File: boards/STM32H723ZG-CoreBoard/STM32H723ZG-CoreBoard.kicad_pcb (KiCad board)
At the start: 4 copper layers, 84 x 84 mm, 48 parts, among them J1 USB-C, J2 PORT_L, J3 PORT_B, J4 PORT_R, J5 PORT_T, J6 SWD, SW1 RESET, SW2 BOOT0, U1 STM32H723ZGT6, U2 AP2112K-3.3, Y1 25MHz, Y2 32.768kHz

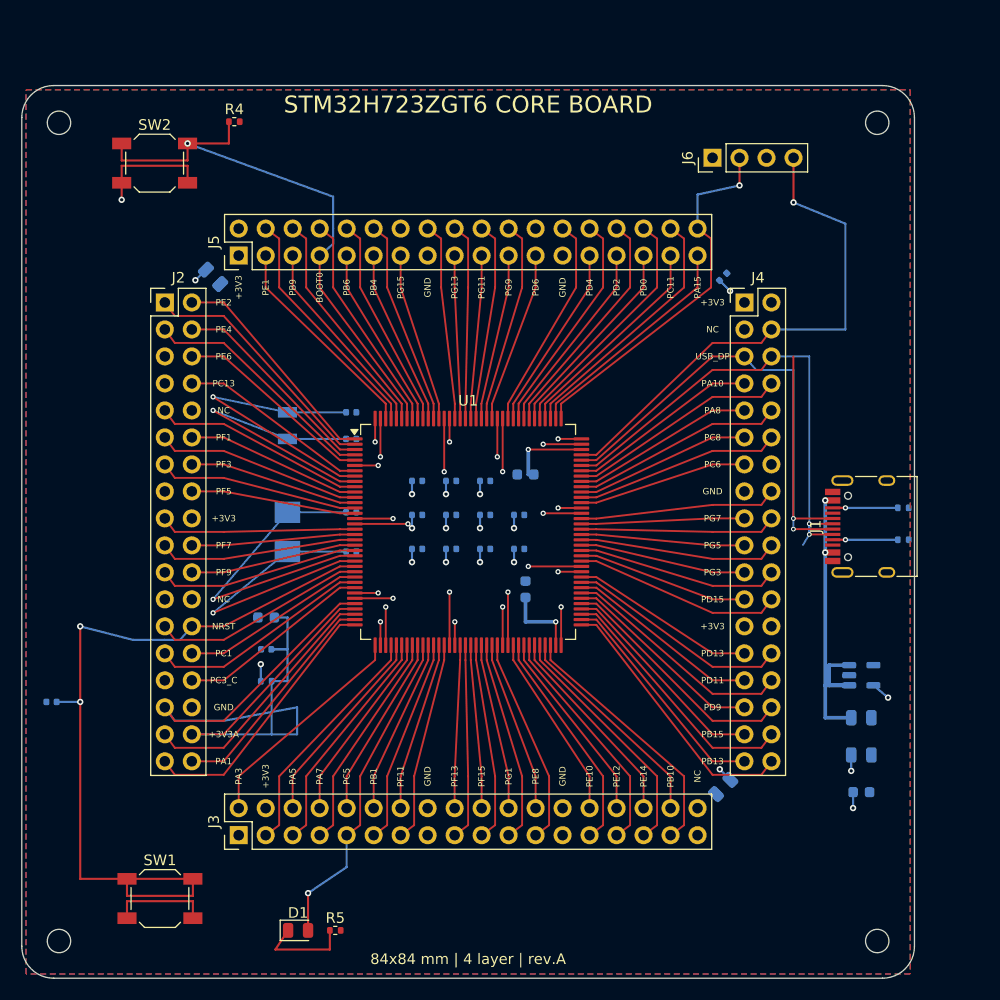
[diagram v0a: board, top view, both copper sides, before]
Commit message: Довести H723 до KiCad 10: разъём прошивки, STDC14, переразметка верхнего кольца
Плата H723 пересобрана в формате KiCad 10 и подтянута к раскладке G474.

Плата:
- разъём прошивки J6 - 1x10 с распиновкой WeAct, развёрнут 5V к востоку,
  SWO садится на PB3 прямой дорожкой;
- добавлен J7 - STDC14 (2x7, 1.27 мм), штатный разъём ST-LINK V3. Стоит
  вертикально сигнальным рядом к J6: строки веера идут по строкам падов и
  между собой не пересекаются, а расходятся по слоям;
- USB-C стоит на плате целиком, D+/D- заведены на PA11/PA12;
- кнопки RST и BOOT0 собраны в колонку у левого края, R4 - вплотную к SW2;
- светодиод и резистор развёрнуты под 45 градусов в углу между J2 и J3;
- подписаны все 144 контакта гребёнок и номиналы всех компонентов.

Генератор:
- gen/kicadenv.py - поиск библиотек KiCad на любой ОС и различия API 7/10;
- gen/export.py - гербера, сверловка, pos.csv, PDF и архив через kicad-cli;
- сборка платы больше не зависит от системных библиотек: футпринты уходят в
  auto_probe.pretty рядом с платой;
- kigen.py: разбор многострочной формы pin_names/pin_numbers KiCad 10 -
  из-за неё поверх номеров контактов печатались имена;
- crtyd.py считает пересечение реальных полигонов, а не описанных
  прямоугольников; drc.py не считает нарушением зазор ровно по правилу.

Проверки H723: DRC KiCad 0 нарушений, 0 несоединённых, 0 расхождений со
схемой; собственный контроль зазоров 0, courtyard 0, шелкография 0.
Файлы платы G474 не тронуты, правки в build_g474.py - только переносимость.

Co-Authored-By: Claude Opus 5 <noreply@anthropic.com>
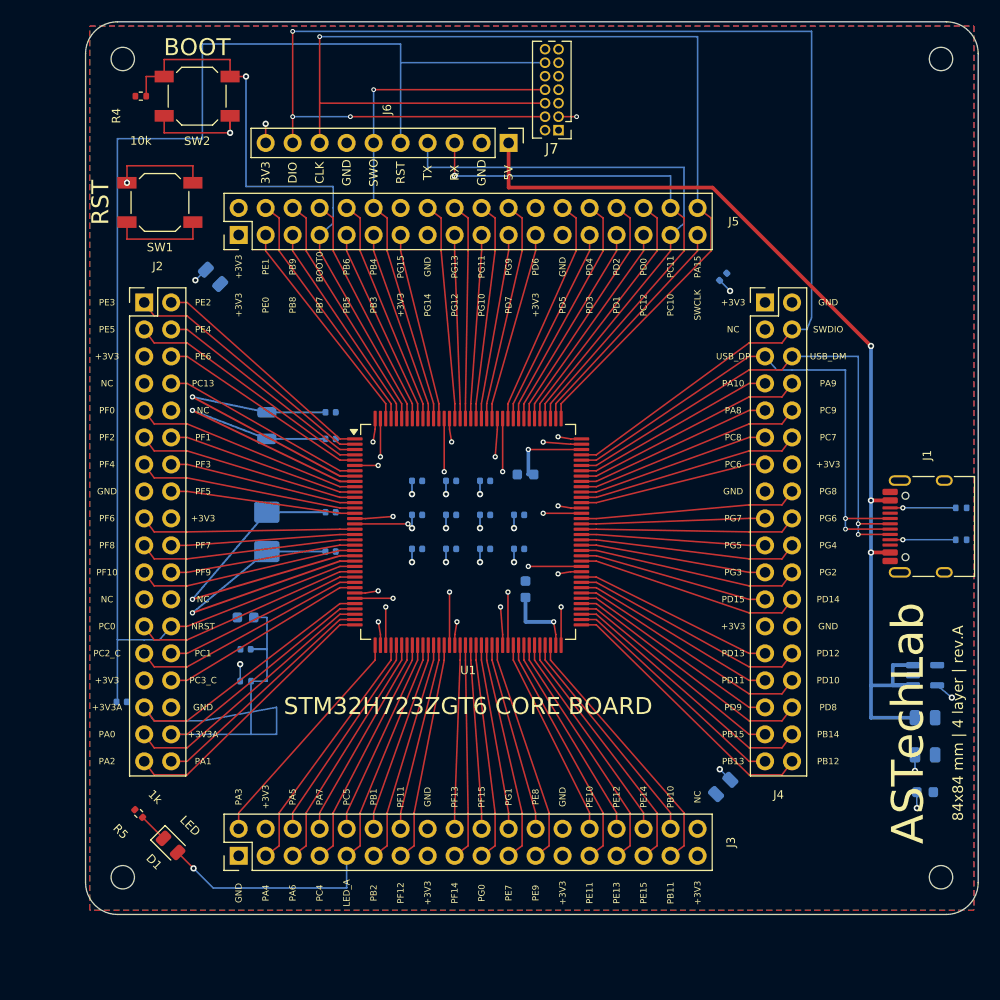
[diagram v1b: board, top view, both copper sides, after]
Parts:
- added J7: STDC14, auto_probe:PinHeader_2x07_P1.27mm_Vertical, F.Cu at (158.5, 62.2)
- C1, C10, C11, C2, C3, C4, C5, C6, C60, C61, C62, C63, C7, C70, C74, C77, C8, C9: footprint C_0402_1005Metric -> auto_probe:C_0402_1005Metric
- C50, C51, C75, C76: footprint C_0805_2012Metric -> auto_probe:C_0805_2012Metric
- C52, C71, C72, C73: footprint C_0603_1608Metric -> auto_probe:C_0603_1608Metric
- D1: value USER -> LED; footprint LED_0805_2012Metric -> auto_probe:LED_0805_2012Metric
- H1, H2, H3, H4: footprint MountingHole_2.2mm_M2 -> auto_probe:MountingHole_2.2mm_M2
- J1: footprint USB_C_Receptacle_HRO_TYPE-C-31-M-12 -> auto_probe:USB_C_Receptacle_HRO_TYPE-C-31-M-12
- J2, J3, J4, J5: footprint PinHeader_2x18_P2.54mm_Vertical -> auto_probe:PinHeader_2x18_P2.54mm_Vertical
- J6: value SWD -> DEBUG; footprint PinHeader_1x04_P2.54mm_Vertical -> auto_probe:PinHeader_1x10_P2.54mm_Vertical
- R1, R2, R3, R4, R5: footprint R_0402_1005Metric -> auto_probe:R_0402_1005Metric
- SW1, SW2: footprint SW_SPST_SKQG_WithoutStem -> auto_probe:SW_SPST_SKQG_WithoutStem
- U1: footprint LQFP-144_20x20mm_P0.5mm -> auto_probe:LQFP-144_20x20mm_P0.5mm
- U2: footprint SOT-23-5 -> auto_probe:SOT-23-5
- Y1: footprint Crystal_SMD_5032-2Pin_5.0x3.2mm -> auto_probe:Crystal_SMD_5032-2Pin_5.0x3.2mm
- Y2: footprint Crystal_SMD_MicroCrystal_CC7V-T1A-2Pin_3.2x1.5mm -> auto_probe:Crystal_SMD_MicroCrystal_CC7V-T1A-2Pin_3.2x1.5mm
- moved SW1 65.5 mm to (121.0, 69.0)
- moved R5 21.5 mm to (119.0, 126.5), turned to 135 degrees
- moved J6 19.2 mm to (153.8, 63.4), turned to -90 degrees
- moved D1 14.4 mm to (122.0, 129.5), turned to -45 degrees
- moved R4 9.12 mm to (119.2, 59.0), turned to 180 degrees
- moved H1 8.49 mm to (117.5, 55.5)
- moved H2 8.49 mm to (117.5, 132.5)
- moved H3 8.49 mm to (194.5, 132.5)
- moved H4 8.49 mm to (194.5, 55.5)
- moved SW2 7.46 mm to (124.5, 59.0)
- moved C77 6.60 mm to (117.4, 116.0), turned to 0 degrees
- moved C50 6.00 mm to (193.0, 117.5)
- moved C51 6.00 mm to (193.0, 121.0)
- moved C52 6.00 mm to (193.0, 124.5)
- moved U2 6.00 mm to (193.0, 113.5)
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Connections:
- J6 pad 1: +3V3 -> VBUS
- J6 pad 2: SWCLK -> GND
- J6 pad 3: GND -> PC10
- J6 pad 4: SWDIO -> PC11
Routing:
- net SWDIO: track 49.1 -> 136.5 mm, vias 1 -> 3
- net SWCLK: track 35.3 -> 109.1 mm
- net NRST: track 73.9 -> 145.8 mm, vias 2 -> 1
- net VBUS: track 32.3 -> 96.8 mm, vias 2 -> 3
- net PC11: track 20.5 -> 54.9 mm
- net PB3: track 19.4 -> 48.4 mm, vias 0 -> 1
- net PC10: track 24.2 -> 51.6 mm, vias 0 -> 1
- net LED_A: track 30.9 -> 41.9 mm
- net USB_DP: track 61.9 -> 51.8 mm
- net LED_K: track 9.09 -> 2.80 mm
- net +3V3: track 83.0 -> 86.5 mm, vias 34 -> 35
- net BOOT0: track 54.1 -> 57.6 mm
- net USB_DM: track 48.6 -> 52.0 mm
- net +3V3A: track 86.1 -> 88.2 mm
- net PG12: track 18.5 -> 20.5 mm
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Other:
- board text added: "0R"
- board text added: "100nF"
- board text added: "10k"
- board text added: "10pF"
- board text added: "10uF"
- board text added: "1k"
- board text added: "1uF"
- board text added: "2.2uF"
- board text added: "25MHz"
- board text added: "32.768kHz"
- board text added: "3V3"
- board text added: "4.7uF"
- board text added: "5.1k"
- board text added: "5V"
- board text added: "6.8pF"
- board text added: "AP2112K-3.3"
- board text added: "ASTechLab"
- board text added: "BOOT"
- board text added: "CLK"
- board text added: "DIO"
- board text added: "LED"
- board text added: "LED_A"
- board text added: "PA0"
- board text added: "PA2"
- board text added: "PA4"
- board text added: "PA6"
- board text added: "PA9"
- board text added: "PB11"
- board text added: "PB12"
- board text added: "PB14"
- board text added: "PB2"
- board text added: "PB3"
- board text added: "PB5"
- board text added: "PB7"
- board text added: "PB8"
- board text added: "PC0"
- board text added: "PC10"
- board text added: "PC12"
- board text added: "PC2_C"
- board text added: "PC4"
- board text added: "PC7"
- board text added: "PC9"
- board text added: "PD1"
- board text added: "PD10"
- board text added: "PD12"
- board text added: "PD14"
- board text added: "PD3"
- board text added: "PD5"
- board text added: "PD7"
- board text added: "PD8"
- board text added: "PE0"
- board text added: "PE11"
- board text added: "PE13"
- board text added: "PE15"
- board text added: "PE3"
- board text added: "PE5"
- board text added: "PE7"
- board text added: "PE9"
- board text added: "PF0"
- board text added: "PF10"
- board text added: "PF12"
- board text added: "PF14"
- board text added: "PF2"
- board text added: "PF4"
- board text added: "PF6"
- board text added: "PF8"
- board text added: "PG0"
- board text added: "PG10"
- board text added: "PG12"
- board text added: "PG14"
- board text added: "PG2"
- board text added: "PG4"
- board text added: "PG6"
- board text added: "PG8"
- board text added: "RST"
- board text added: "RX"
- board text added: "SWCLK"
- board text added: "SWDIO"
- board text added: "SWO"
- board text added: "TX"
- board text added: "USB_DM"

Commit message: H723: убрать STDC14, переразметить верхнее кольцо и шелкографию под нормы печати
Разъём прошивки и его окружение:
- STDC14 (J7) снят с платы, из схемы и из библиотеки проекта: вертикально он
  занимал 7.6 мм по высоте и не давал поднять J6;
- J6 поднят к верхнему краю (Y0+5.2), обозначение закреплено в торце справа;
- полосы SWO/CLK/DIO отведены от контура: было 0.67 мм до фрезы, стало 1.67;
- BOOT0 к гребёнке обходит J6 западнее, отвод +3V3 от контакта 10 смотрит вверх.

Шелкография приведена к нормам JLCPCB (0.8 мм при линии 0.15):
- подписи контактов были 0.6/0.1, номиналы на обратной стороне 0.5 - мельче
  минимума, при печати такие символы плывут;
- строки подписей отодвинуты от гребёнок, внешние выставлены по центру кольца:
  крупный шрифт задевал контур разъёма и свешивался за край платы;
- в кольце 3.7 мм, пятизначное имя туда не входит - для нескольких цепей на
  шелке короткая форма (3V3A, PC2C, USBDP); в схеме и PINOUT.csv имена полные;
- у деталей печатается только обозначение, номиналы собраны в таблицу
  "обозначение - номинал" на 35 строк в двух свободных площадках у J4;
- обозначение ставится строго над своей деталью горизонтально: раньше список
  занятых мест включал их же штатные позиции, подпись конфликтовала сама с
  собой и уезжала в сторону под произвольным углом.

Расхождения со схемой (видны только в GUI, CLI их не показывает):
- висящим выводам проставлены те же имена, что генерирует eeschema
  (unconnected-(REF-ИМЯ-PadN)) - 9 штук;
- крепёжные отверстия добавлены в схему, с футпринта снята пометка "не в BOM";
- номинал R3 в схеме сведён с платой (0R/FB).

Развязка: C74 перенесён от края к своему выводу VDD33USB (было 25.5 мм, стало
5.9), места в сетке под корпусом раздаются по близости к своему выводу
(в среднем 12.4 -> 9.4 мм).

silkchk.py теперь ловит шелк за контуром платы - KiCad этого не проверяет.

Проверки H723: DRC KiCad 0 нарушений и 0 предупреждений, 0 несоединённых,
0 расхождений со схемой; свой контроль зазоров 0, courtyard 0, ш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
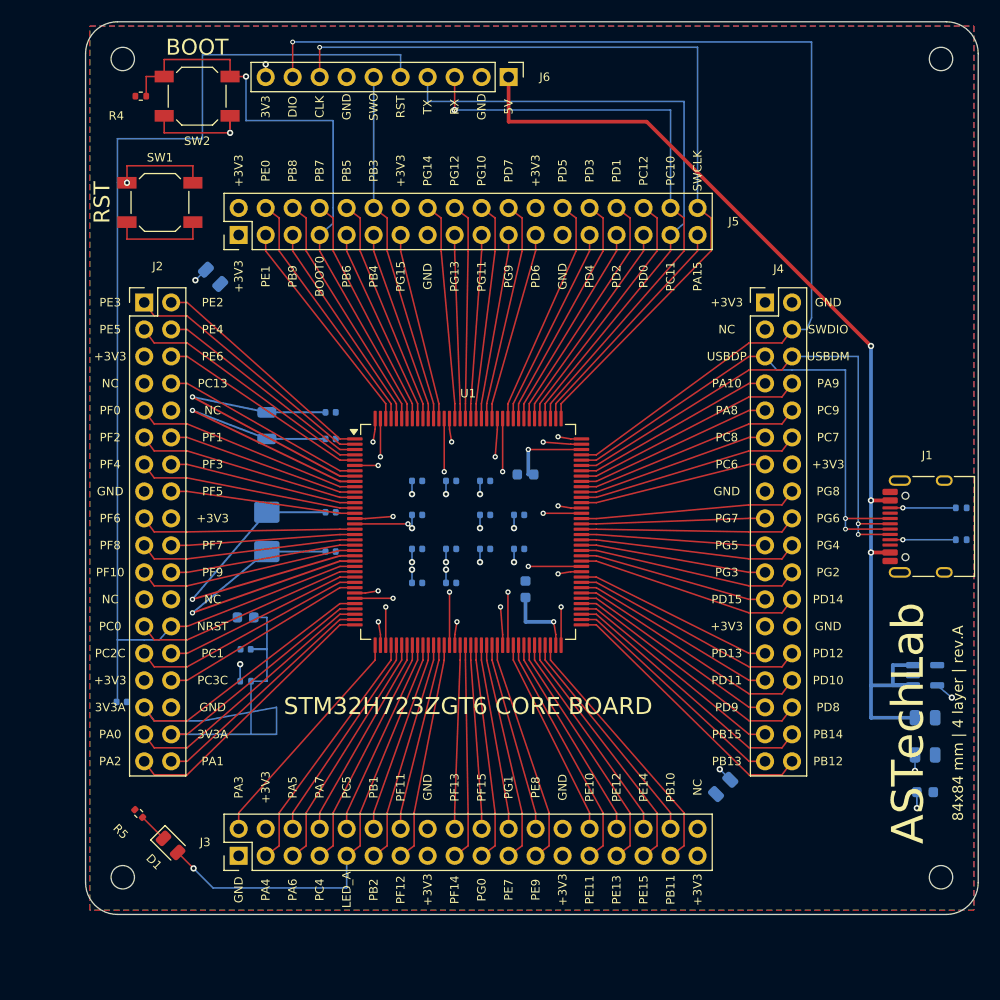
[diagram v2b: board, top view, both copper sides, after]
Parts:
- removed J7: STDC14, auto_probe:PinHeader_2x07_P1.27mm_Vertical
- moved C74 29.5 mm to (154.8, 98.4), turned to 0 degrees
- moved C11 11.5 mm to (145.2, 95.2)
- moved C2 10.1 mm to (145.2, 104.8)
- moved C3 9.05 mm to (145.2, 101.6)
- moved C8 7.16 mm to (151.6, 98.4)
- moved C4 7.16 mm to (148.4, 104.8)
- moved C10 7.16 mm to (148.4, 95.2)
- moved C9 7.16 mm to (151.6, 95.2)
- moved J6 6.20 mm to (153.8, 57.2)
- moved C5 4.53 mm to (151.6, 101.6)
- moved C6 4.53 mm to (148.4, 101.6)
- moved C1 3.20 mm to (145.2, 98.4)
- moved C7 3.20 mm to (154.8, 101.6)
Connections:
- J1 pad A8: (no net) -> unconnected-(J1-SBU1-PadA8)
- J1 pad B8: (no net) -> unconnected-(J1-SBU2-PadB8)
- J2 pad 10: (no net) -> unconnected-(J2-Pin_10-Pad10)
- J2 pad 23: (no net) -> unconnected-(J2-Pin_23-Pad23)
- J2 pad 24: (no net) -> unconnected-(J2-Pin_24-Pad24)
- J2 pad 7: (no net) -> unconnected-(J2-Pin_7-Pad7)
- J3 pad 36: (no net) -> unconnected-(J3-Pin_36-Pad36)
- J4 pad 3: (no net) -> unconnected-(J4-Pin_3-Pad3)
- U2 pad 4: (no net) -> unconnected-(U2-NC-Pad4)
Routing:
- net SWDIO: track 136.5 -> 104.6 mm, vias 3 -> 1
- net SWCLK: track 109.1 -> 79.7 mm
- net NRST: track 145.8 -> 124.0 mm
- net PB3: track 48.4 -> 33.4 mm, vias 1 -> 0
- net PC10: track 51.6 -> 57.8 mm
- net PC11: track 54.9 -> 61.1 mm
- net VBUS: track 96.8 -> 99.4 mm
- net +3V3: track 86.5 -> 84.1 mm, vias 35 -> 34
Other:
- board text added: "3V3A"
- board text added: "C1 100nF"
- board text added: "C10 100nF"
- board text added: "C11 100nF"
- board text added: "C2 100nF"
- board text added: "C3 100nF"
- board text added: "C4 100nF"
- board text added: "C5 100nF"
- board text added: "C50 10uF"
- board text added: "C51 10uF"
- board text added: "C52 100nF"
- board text added: "C6 100nF"
- board text added: "C60 10pF"
- board text added: "C61 10pF"
- board text added: "C62 6.8pF"
- board text added: "C63 6.8pF"
- board text added: "C7 100nF"
- board text added: "C70 100nF"
- board text added: "C71 1uF"
- board text added: "C72 2.2uF"
- board text added: "C73 2.2uF"
- board text added: "C74 100nF"
- board text added: "C75 4.7uF"
- board text added: "C76 4.7uF"
- board text added: "C77 100nF"
- board text added: "C8 100nF"
- board text added: "C9 100nF"
- board text added: "D1 LED"
- board text added: "PC2C"
- board text added: "PC3C"
- board text added: "R1 5.1k"
- board text added: "R2 5.1k"
- board text added: "R3 0R/FB"
- board text added: "R4 10k"
- board text added: "R5 1k"
- board text added: "U2 AP2112K-3.3"
- board text added: "USBDM"
- board text added: "USBDP"
- board text added: "Y1 25MHz"
- board text added: "Y2 32.768kHz"
- board text removed: "+3V3A"
- board text removed: "0R"
- board text removed: "100nF"
- board text removed: "10k"
- board text removed: "10pF"
- board text removed: "10uF"
- board text removed: "1k"
- board text removed: "1uF"
- board text removed: "2.2uF"
- board text removed: "25MHz"
- board text removed: "32.768kHz"
- board text removed: "4.7uF"
- board text removed: "5.1k"
- board text removed: "6.8pF"
- board text removed: "AP2112K-3.3"
- board text removed: "LED"
- board text removed: "PC2_C"
- board text removed: "PC3_C"
- board text removed: "USB_DM"
- board text removed: "USB_DP"

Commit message: H723: кварц под наличие JLCPCB, номера LCSC в BOM, выходные файлы в их формате
Кварц HSE переведён на корпус, который у JLCPCB есть как Basic Part:
- Y1 - SMD-3225 с четырьмя падами (Yangxing X322525MOB4SI, C9006) вместо
  двухпадового 5032: тот только Extended и с перебоями в наличии;
- сигнальные пады у 3225 стоят по диагонали, между ними земляные, поэтому оба
  сигнала заходят с запада разными колонками, а отвод HSE_OUT к своей банке
  идёт под корпусом;
- экранные пады связаны диагональю под кварцем и посажены на полигон одной via:
  вокруг проходит веер J2, второй via там не встаёт;
- нагрузочная ёмкость нового кварца 12 пФ, поэтому обвязка обоих генераторов
  пересчитана с 10 и 6.8 пФ на 18 пФ (C60-C63).

Выходные файлы приведены к формату JLCPCB:
- pos.csv переименовывает колонки в Designator / Mid X / Mid Y / Rotation /
  Layer - родные заголовки KiCad их парсер отвергает целиком;
- BOM.csv собран из Comment / Designator / Footprint / LCSC Part #;
- крепёжные отверстия из сборочного BOM убраны: все пады неметаллизированные,
  паять нечего, а JLCPCB ругался на их отсутствие в CPL;
- проставлены номера LCSC на 22 позиции из списка Basic Parts, для кварцев
  вместо номера - требование по нагрузочной ёмкости, для AP2112K - замена по
  выводам ME6211C33M5G-N (C82942) на случай дефицита.

Шелкография: у D1 подписана полярность (+/- сбоку от падов, по цепям LED_A и
LED_K), обозначения деталей ставятся строго над корпусом горизонтально.

Проверки H723: DRC KiCad 0 нарушений и 0 предупреждений, 0 несоединённых,
0 расхождений со схемой; свой контроль зазоров 0, courtyard 0, шелкография
0 наложений, 0 поверх падов, 0 за контуром.

Co-Authored-By: Claude Opus 5 <noreply@anthropic.com>
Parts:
- C60, C61: value 10pF -> 18pF
- C62, C63: value 6.8pF -> 18pF
- Y1: footprint auto_probe:Crystal_SMD_5032-2Pin_5.0x3.2mm -> auto_probe:Crystal_SMD_3225-4Pin_3.2x2.5mm
- moved C60 0.75 mm to (137.1, 98.9)
- moved C61 0.75 mm to (137.1, 101.1)
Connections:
- Y1 pad 2: HSE_OUT -> GND
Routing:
- net HSE_OUT: track 30.7 -> 39.7 mm
- net HSE_IN: track 32.2 -> 39.8 mm
- net GND: track 44.1 -> 48.8 mm, vias 10 -> 11
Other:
- board text added: "+"
- board text added: "-"
- board text added: "C60 18pF"
- board text added: "C61 18pF"
- board text added: "C62 18pF"
- board text added: "C63 18pF"
- board text removed: "C60 10pF"
- board text removed: "C61 10pF"
- board text removed: "C62 6.8pF"
- board text removed: "C63 6.8pF"
